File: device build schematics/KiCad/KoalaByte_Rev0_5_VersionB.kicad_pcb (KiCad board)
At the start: 2 copper layers, 120 x 85 mm, 0 parts

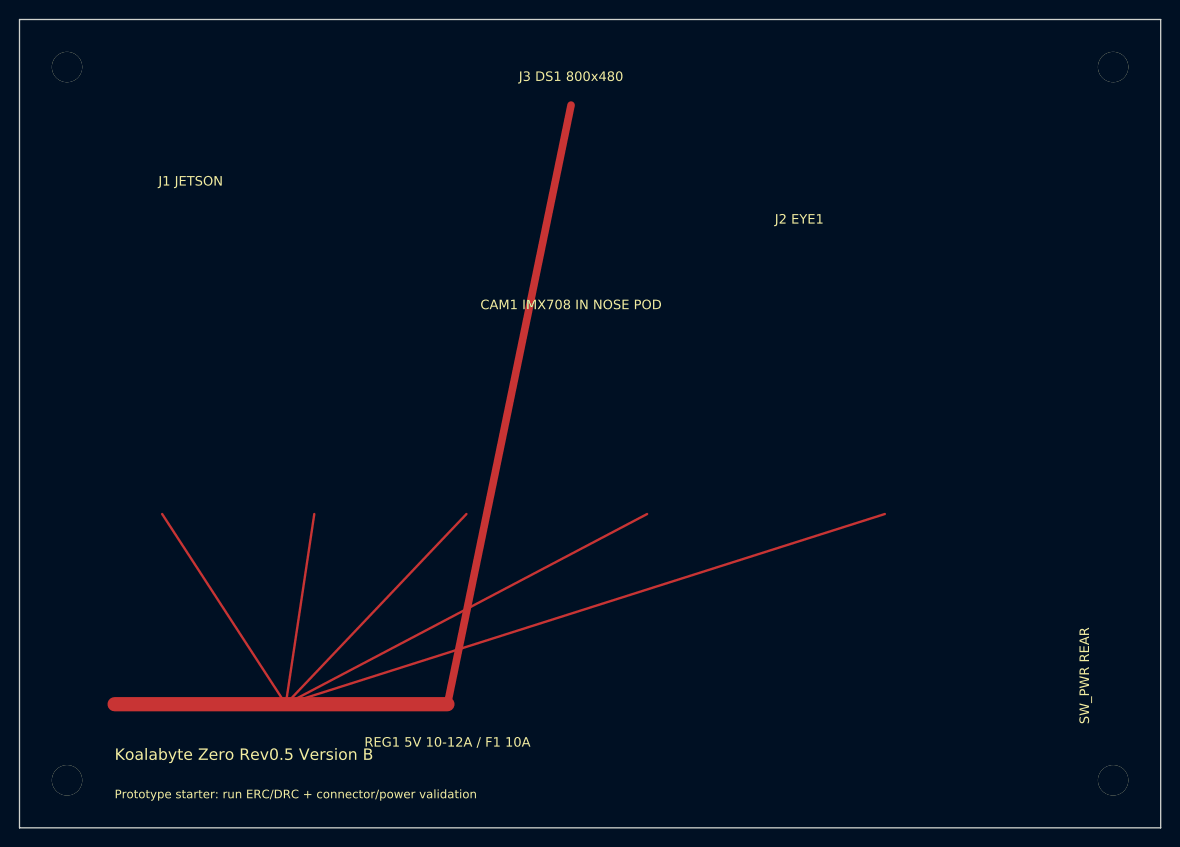
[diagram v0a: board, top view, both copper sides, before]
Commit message: Add MIC1 PCB starter annotation
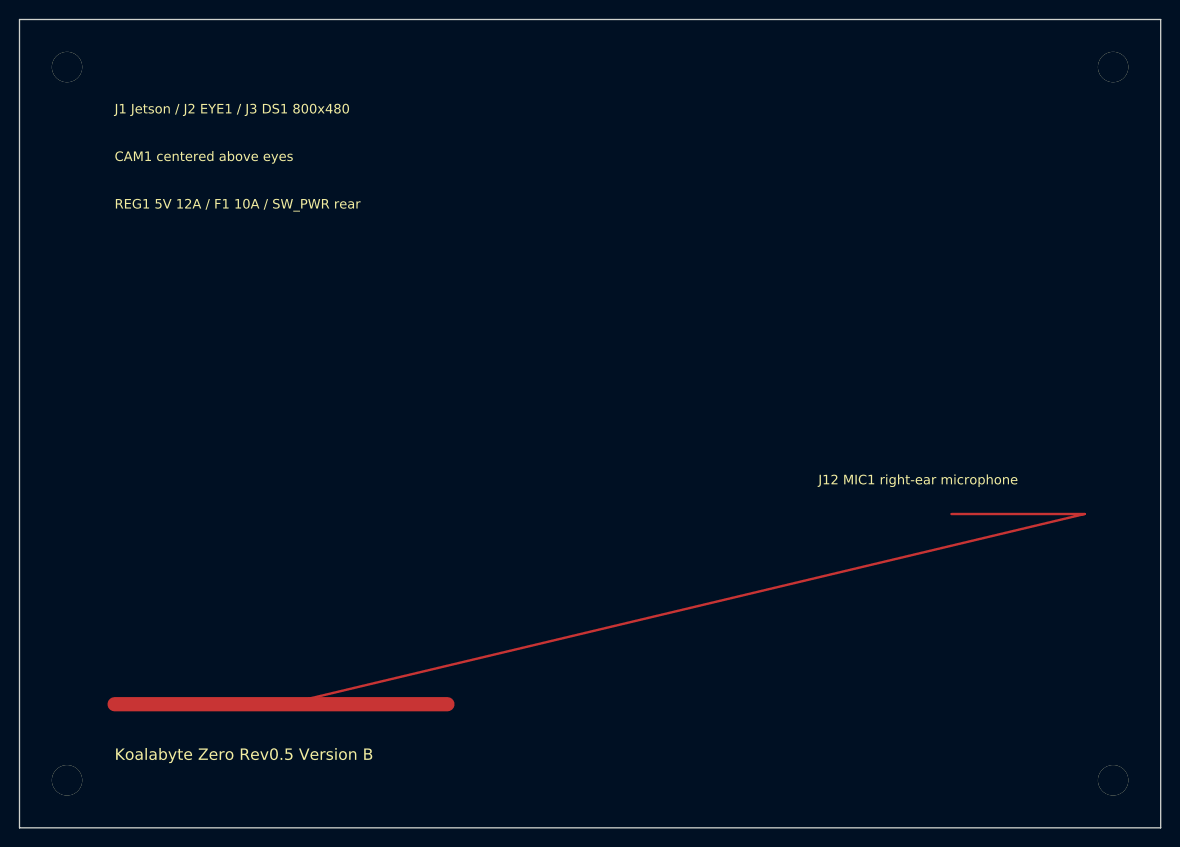
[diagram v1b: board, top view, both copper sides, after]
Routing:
- net +3V3: track 180.7 -> 86.3 mm
- net +5V_MAIN: track 99.3 -> 35.0 mm
- net MIC1_I2S: track 0.00 -> 14.0 mm
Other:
- board text added: "CAM1 centered above eyes"
- board text added: "J1 Jetson / J2 EYE1 / J3 DS1 800x480"
- board text added: "J12 MIC1 right-ear microphone"
- board text added: "REG1 5V 12A / F1 10A / SW_PWR rear"
- board text removed: "CAM1 IMX708 IN NOSE POD"
- board text removed: "J1 JETSON"
- board text removed: "J2 EYE1"
- board text removed: "J3 DS1 800x480"
- board text removed: "Prototype starter: run ERC/DRC + connector/power validation"
- board text removed: "REG1 5V 10-12A / F1 10A"
- board text removed: "SW_PWR REAR"
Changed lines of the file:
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@@
     (company "Urban Poacher / Koalabyte")
     (comment 1 "Prototype interface shield / harness board; not final production verified")
-    (comment 2 "DS1 800x480, CAM1 IMX708, REG1 5V 10-12A, F1 10A-class")
+    (comment 2 "DS1 800x480, CAM1 IMX708, MIC1 right-ear microphone, REG1 5V 12A")
   )
   (layers
     (0 "F.Cu" signal)
     (31 "B.Cu" signal)
-    (32 "B.Adhes" user)
-    (33 "F.Adhes" user)
-    (34 "B.Paste" user)
-    (35 "F.Paste" user)
-    (36 "B.SilkS" user)
     (37 "F.SilkS" user)
-    (38 "B.Mask" user)
     (39 "F.Mask" user)
     (44 "Edge.Cuts" user)
-  )
-  (setup
-    (stackup
-      (layer "F.SilkS" (type "Top Silk Screen"))
-      (layer "F.Paste" (type "Top Solder Paste"))
-      (layer "F.Mask" (type "Top Solder Mask") (thickness 0.01))
-      (layer "F.Cu" (type "copper") (thickness 0.035))
-      (layer "dielectric 1" (type "core") (thickness 1.51) (material "FR4") (epsilon_r 4.5) (loss_tangent 0.02))
-      (layer "B.Cu" (type "copper") (thickness 0.035))
-      (layer "B.Mask" (type "Bottom Solder Mask") (thickness 0.01))
-      (layer "B.Paste" (type "Bottom Solder Paste"))
-      (layer "B.SilkS" (type "Bottom Silk Screen"))
-    )
-    (pad_to_mask_clearance 0)
-    (solder_mask_min_width 0)
-    (aux_axis_origin 0 0)
-    (grid_origin 0 0)
   )
   (net 0 "")
@@
   (net 14 "CC1101_CS")
   (net 15 "BUTTON_BUS")
+  (net 16 "MIC1_I2S")
   (gr_rect (start 0 0) (end 120 85) (stroke (width 0.1) (type default)) (fill none) (layer "Edge.Cuts"))
-  (gr_text "Koalabyte Zero Rev0.5 Version B" (at 10 78 0) (layer "F.SilkS")
-    (effects (font (size 1.2 1.2) (thickness 0.15)) (justify left bottom))
-  )
-  (gr_text "Prototype starter: run ERC/DRC + connector/power validation" (at 10 82 0) (layer "F.SilkS")
-    (effects (font (size 0.9 0.9) (thickness 0.12)) (justify left bottom))
-  )
-  (gr_text "J1 JETSON" (at 18 17 0) (layer "F.SilkS")
-    (effects (font (size 1 1) (thickness 0.12)))
-  )
-  (gr_text "J2 EYE1" (at 82 21 0) (layer "F.SilkS")
-    (effects (font (size 1 1) (thickness 0.12)))
-  )
-  (gr_text "J3 DS1 800x480" (at 58 6 0) (layer "F.SilkS")
-    (effects (font (size 1 1) (thickness 0.12)))
-  )
-  (gr_text "SW_PWR REAR" (at 112 69 90) (layer "F.SilkS")
-    (effects (font (size 1 1) (thickness 0.12)))
-  )
-  (gr_text "CAM1 IMX708 IN NOSE POD" (at 58 30 0) (layer "F.SilkS")
-    (effects (font (size 1 1) (thickness 0.12)))
-  )
-  (gr_text "REG1 5V 10-12A / F1 10A" (at 45 76 0) (layer "F.SilkS")
-    (effects (font (size 1 1) (thickness 0.12)))
-  )
+  (gr_text "Koalabyte Zero Rev0.5 Version B" (at 10 78 0) (layer "F.SilkS") (effects (font (size 1.2 1.2) (thickness 0.15)) (justify left bottom)))
+  (gr_text "J1 Jetson / J2 EYE1 / J3 DS1 800x480" (at 10 10 0) (layer "F.SilkS") (effects (font (size 1 1) (thickness 0.12)) (justify left bottom)))
+  (gr_text "CAM1 centered above eyes" (at 10 15 0) (layer "F.SilkS") (effects (font (size 1 1) (thickness 0.12)) (justify left bottom)))
+  (gr_text "J12 MIC1 right-ear microphone" (at 84 49 0) (layer "F.SilkS") (effects (font (size 1 1) (thickness 0.12)) (justify left bottom)))
+  (gr_text "REG1 5V 12A / F1 10A / SW_PWR rear" (at 10 20 0) (layer "F.SilkS") (effects (font (size 1 1) (thickness 0.12)) (justify left bottom)))
   (segment (start 10 72) (end 45 72) (width 1.5) (layer "F.Cu") (net 1))
-  (segment (start 45 72) (end 58 9) (width 0.8) (layer "F.Cu") (net 1))
-  (segment (start 28 72) (end 15 52) (width 0.25) (layer "F.Cu") (net 2))
-  (segment (start 28 72) (end 31 52) (width 0.25) (layer "F.Cu") (net 2))
-  (segment (start 28 72) (end 47 52) (width 0.25) (layer "F.Cu") (net 2))
-  (segment (start 28 72) (end 66 52) (width 0.25) (layer "F.Cu") (net 2))
-  (segment (start 28 72) (end 91 52) (width 0.25) (layer "F.Cu") (net 2))
+  (segment (start 28 72) (end 112 52) (width 0.25) (layer "F.Cu") (net 2))
+  (segment (start 112 52) (end 98 52) (width 0.25) (layer "F.Cu") (net 16))
   (via (at 5 5) (size 3.2) (drill 3.2) (layers "F.Cu" "B.Cu") (net 3))
   (via (at 115 5) (size 3.2) (drill 3.2) (layers "F.Cu" "B.Cu") (net 3))
